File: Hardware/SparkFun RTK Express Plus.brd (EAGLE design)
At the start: 68.2 x 110.1 mm, 171 parts, among them J13 Internal, J16 MICRO-SD-PUSH-PUSH-EXT-PIN, J17 Qwiic Right Angle, J3 USB Female Type C Connector, J4 External, J5 USB Female Type C Connector, Q1 SIL2308-TP, Q2 MBT3904DW1T1, U1 74HC4052D, U10 MCP73833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

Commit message: v13 PCB - LIF connector, accel ground plane, ESP32 FP.
* Removed ground plane from around the accel to aid in reflow and rework
* Route out text in screw areas
* New 6 pin overlay connector
* ENIG finish
* Full ESP32 FP
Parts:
- removed J20: (no value), RTK Facet:FPC_12_DOUBLESIDED_BACKFLIP
- removed U$19: (no value), output:V120
- added J19: (no value), SparkFun-Connectors:FPC_6_1MM-LIF
- added U$1: (no value), output:V130
- D10: value PESD0402 -> PESD0402-0402
- JP1: value (none) -> JUMPER-SMT_2_NO_SILK
- MEAS, MEAS1: value (none) -> JUMPER-COMBO_2_NC_TRACE
- U5: value ESP-WROOM-3232D-NARROW -> ESP-WROOM-3232D; device SparkFun-RF:ESP-WROOM-32D-NARROW -> SparkFun-RF:ESP-WROOM-32D
- moved U$8 3.00 mm to (52.0, 103.0)
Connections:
- net CHG_LED_RES: now also J19.2; no longer J20.3, J20.4
- net ESP_14/SETUP_BUTTON: now also J19.4; no longer J20.7, J20.8
- net GND: now also J19.6, U5.GND; no longer J20.11, J20.12, U5.GND1
- net POWER_BTN: now also J19.5; no longer J20.10, J20.9
- net V_USB: now also J19.1; no longer J20.1, J20.2
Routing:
- net CHG_LED_RES: track 26.4 -> 24.1 mm
- net ESP32_EN: track 74.2 -> 76.4 mm
- net V_USB: track 135.3 -> 133.9 mm
- net POWER_BTN: track 139.5 -> 138.0 mm
- net ESP_14/SETUP_BUTTON: track 31.7 -> 30.8 mm
- net ESP32_RXI: track 8.67 -> 7.91 mm
- net N$6: track 42.0 -> 41.3 mm
- net ESP_I35/DEVICE_SENSE: track 18.9 -> 19.6 mm
- net ESP_I16/ZED-TXO1: track 110.0 -> 110.8 mm
- net ESP_4/MUX_B: track 41.8 -> 42.6 mm
- net ESP_27/FAST_OFF: track 52.5 -> 53.2 mm
- net ESP_26/DAC2: track 36.3 -> 37.1 mm
- net ESP_23/COPI: track 112.7 -> 111.9 mm
- net ESP_22/SCL: track 212.3 -> 211.5 mm
- net ESP_21/SDA: track 209.4 -> 210.2 mm
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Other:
- board text added: "ENIG Finish"
- board text added: "Red Soldermask"

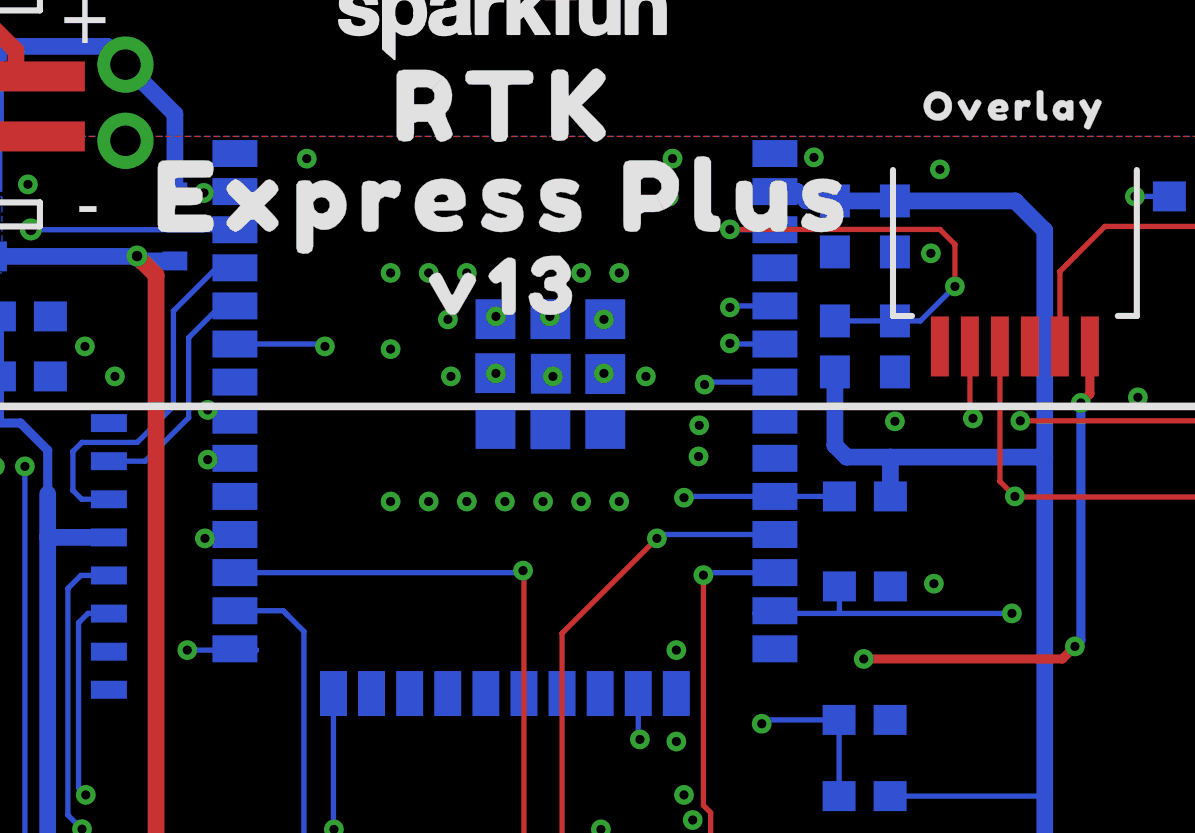
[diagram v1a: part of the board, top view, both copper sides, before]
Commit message: v13 - Change to LIF overlay connector. Change ESP32 FP. Pull ground from accel.
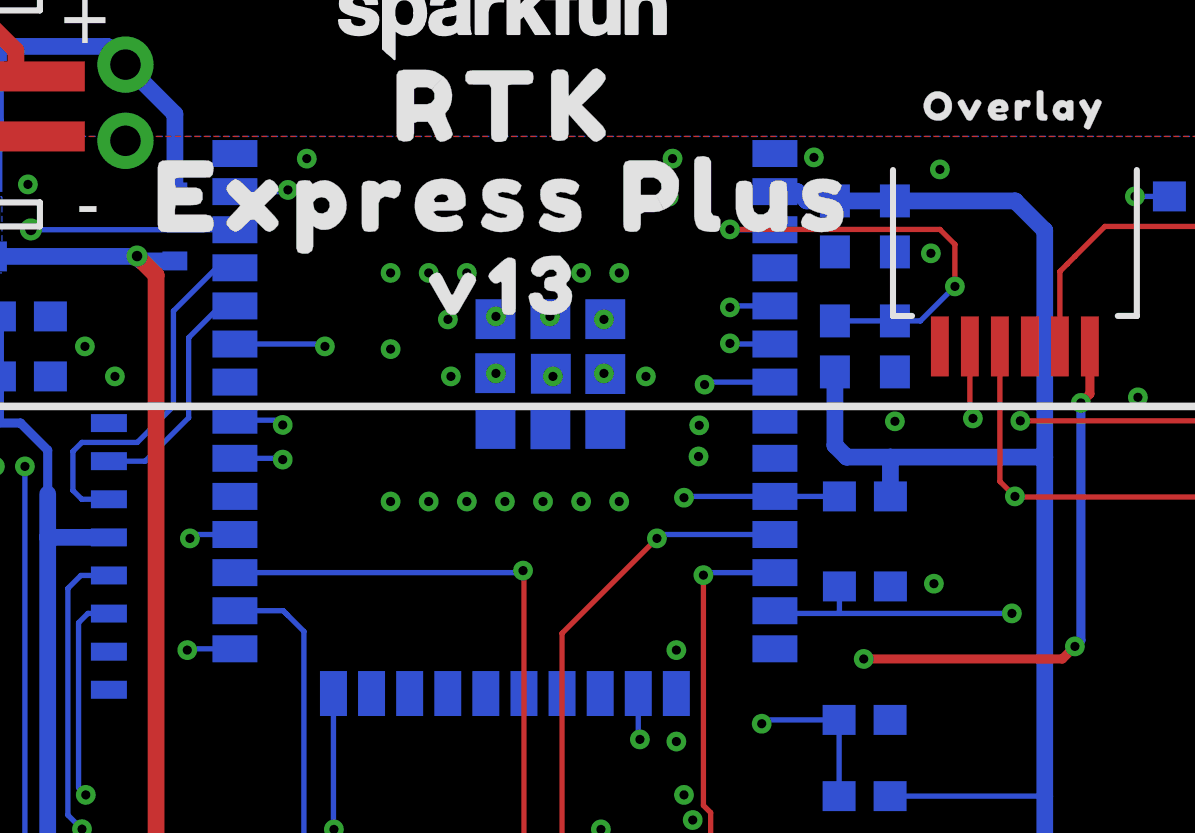
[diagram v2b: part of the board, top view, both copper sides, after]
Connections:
- net ESP_19/CIPO renamed ESP_19/POCI
- net ESP_23/COPI renamed ESP_23/PICO
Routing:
- net ESP_19/POCI: track 109.3 -> 107.2 mm
- net ESP_23/PICO: track 111.9 -> 109.9 mm
- net ESP_18/SCK: track 105.9 -> 104.1 mm
- net ESP_0/BOOT: track 15.1 -> 13.7 mm
- net ESP_14/SETUP_BUTTON: track 30.8 -> 29.5 mm
- net N$6: track 41.3 -> 42.0 mm
